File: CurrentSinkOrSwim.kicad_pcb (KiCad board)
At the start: 2 copper layers, 57.1 x 64 mm, 35 parts, among them P1 HEATSINK, P101 CONN_01X02, P102 CONN_01X03, P103 CONN_01X02, Q401 BUK9575, U201 LMV358, U301 LM2931

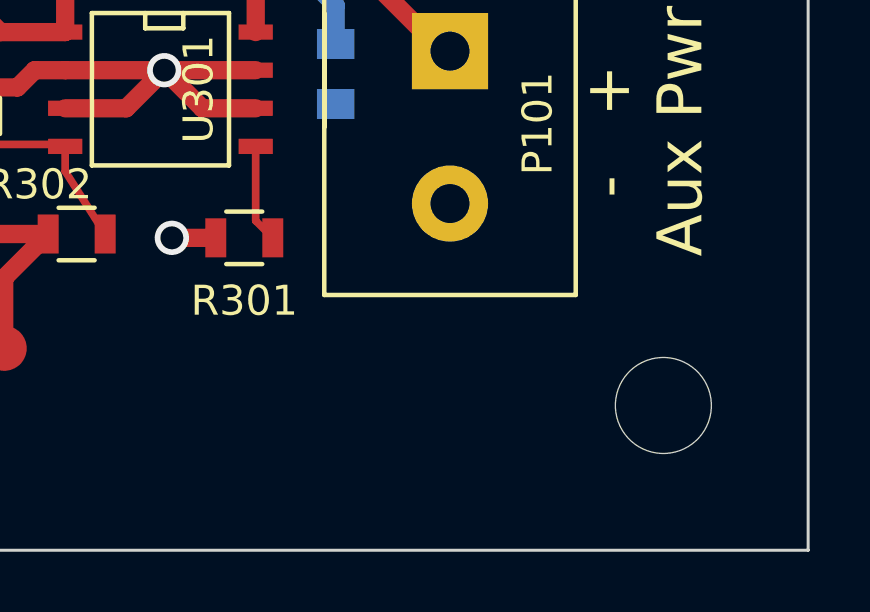
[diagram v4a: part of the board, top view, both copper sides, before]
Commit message: added test point for GND
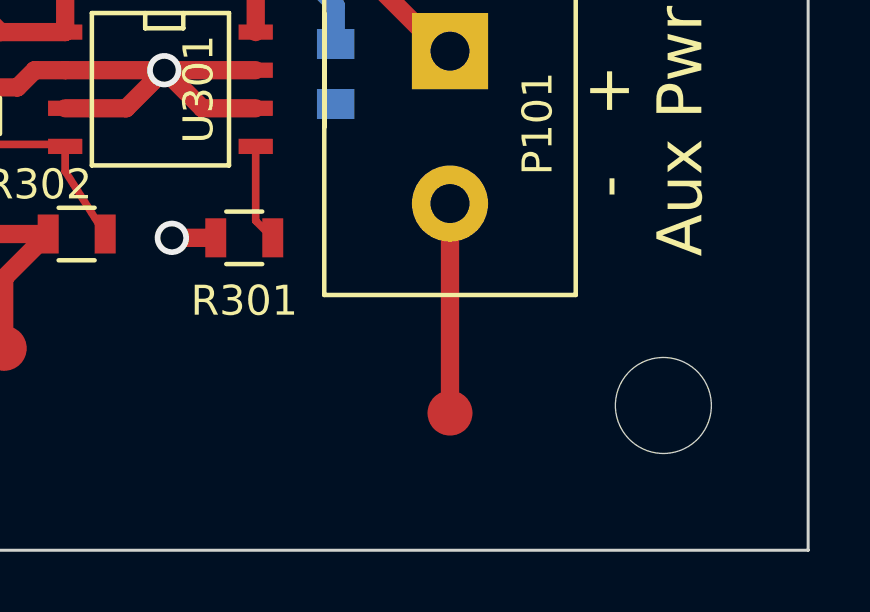
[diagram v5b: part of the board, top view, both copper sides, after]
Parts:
- added W102: TEST_1P, Measurement_Points:Measurement_Point_Round-SMD-Pad_Small, F.Cu at (143.6, 87.5)
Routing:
- net GND: track 41.0 -> 48.0 mm
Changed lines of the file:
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@@
 (kicad_pcb (version 4) (host pcbnew 4.0.2-stable)
   (general
-    (links 51)
+    (links 52)
     (no_connects 0)
-    (area 93.514057 27.4632 160.485943 92.5288)
+    (area 98.374999 28.016999 155.625001 92.125001)
     (thickness 1.6)
     (drawings 8)
-    (tracks 146)
+    (tracks 147)
     (zones 0)
-    (modules 35)
+    (modules 36)
     (nets 17)
   )
@@
     )
   )
+  (module Measurement_Points:Measurement_Point_Round-SMD-Pad_Small (layer F.Cu)
+    (at 143.637 87.503)
+    (descr "Mesurement Point, Round, SMD Pad, DM 1.5mm,")
+    (tags "Mesurement Point Round SMD Pad 1.5mm")
+    (attr virtual)
+    (fp_text reference W102 (at 0 -2) (layer F.SilkS) hide
+      (effects (font (size 1 1) (thickness 0.15)))
+    )
+    (fp_text value TEST_1P (at 0 2) (layer F.Fab)
+      (effects (font (size 1 1) (thickness 0.15)))
+    )
+    (fp_circle (center 0 0) (end 1 0) (layer F.CrtYd) (width 0.05))
+    (pad 1 smd circle (at 0 0) (size 1.5 1.5) (layers F.Cu F.Mask)
+      (net 2 GND))
+  )
   (gr_text "-     +\nVoltageCtrl" (at 103.505 68.453 270) (layer F.SilkS)
     (effects (font (size 1.5 1.5) (thickness 0.3)))
@@
   (segment (start 130.241 81.534) (end 127.753 81.534) (width 0.6096) (layer F.Cu) (net 1) (status 10))
   (segment (start 127.753 81.534) (end 122.809 76.59) (width 0.6096) (layer F.Cu) (net 1))
+  (segment (start 143.637 80.518) (end 143.637 87.503) (width 0.6096) (layer F.Cu) (net 2) (status 20))
   (segment (start 131.699 62.028) (end 132.64 62.028) (width 0.6096) (layer F.Cu) (net 2))
   (segment (start 132.64 62.028) (end 134.366 63.754) (width 0.6096) (layer F.Cu) (net 2))
